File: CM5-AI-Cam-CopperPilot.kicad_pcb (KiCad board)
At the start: 6 copper layers, 55 x 40 mm, 90 parts, among them J1 IMX219_30P, J2 USB_A_Vertical, Q1 DMG1012T, Q2 DMG1012T, U1 RT9193-28GB, U2 RT9193-18GB, U3 RT9013-12, U4 STMPS2171STR, U5 MP1658GTF-Z, U6 FSUSB42MX, U7 STMPS2171STR, U8 STMPS2171STR, X1 OSC_24MHz

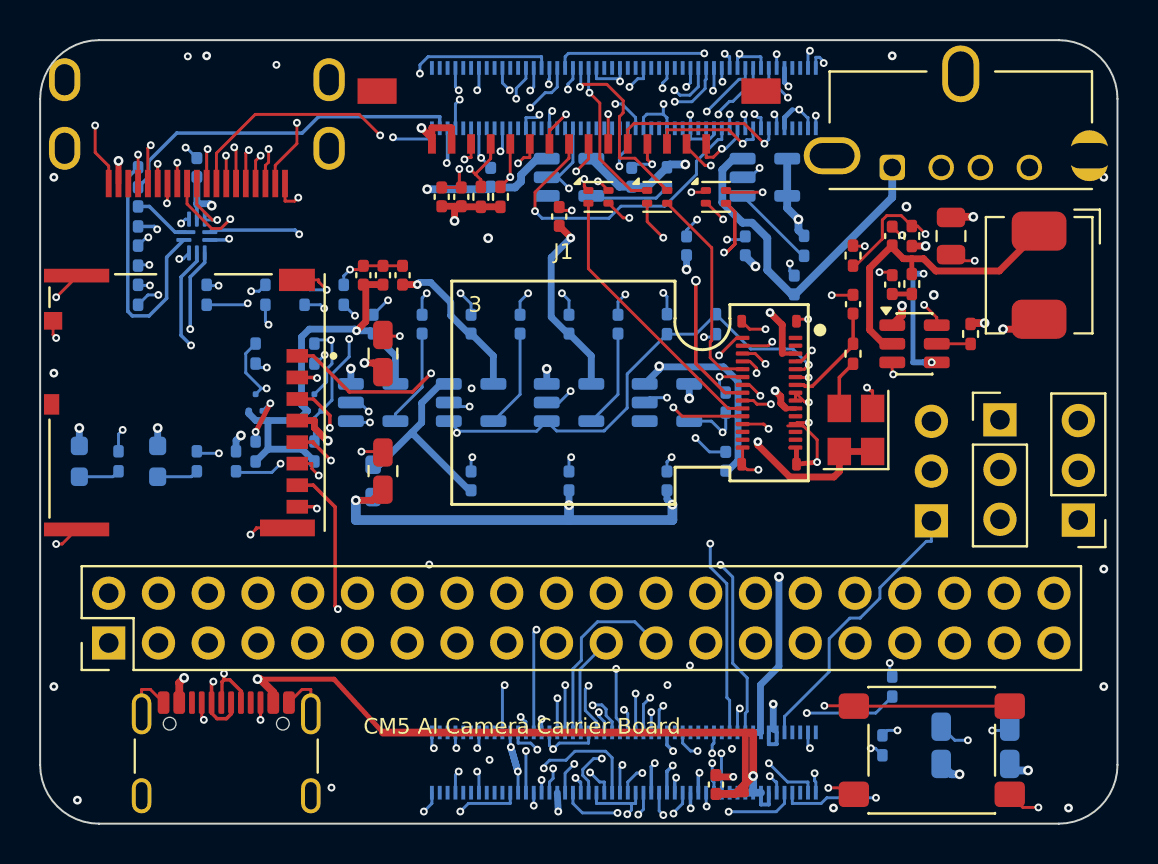
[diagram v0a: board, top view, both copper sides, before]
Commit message: fix(hardware): separate 100R MIPI/HDMI and 90R USB netclasses and resolve BOM/SCH/PCB review defects
- Assign HighSpeed_100R (100 Ohm diff: W=0.127mm, S=0.150mm -> 100.1 Ohm on JLC06161H-7628 stripline / 98.3 Ohm on JLC06161H-3313 microstrip) to MIPI CSI-2, MIPI DSI, and HDMI TMDS pairs, and HighSpeed_90R (90 Ohm diff: W=0.180mm, S=0.150mm -> 89.6 Ohm stripline / 88.7 Ohm microstrip) to USB 2.0 pairs in .kicad_pro, .kicad_pcb, and .kicad_dru.
- Synchronize .kicad_pcb stackup dielectric parameters with JLCPCB JLC06161H-7628 (0.2104mm prepreg, 0.4000mm core, er=4.6).
- Restore C20 on 24 MHz camera MCLK from 0.1uF (72.3 kHz cutoff) to 10pF (C32949, fc=723 MHz) and correct LCSC codes for R20 (C25803 61.9k), U3 (C47773 1.2V LDO), U1 (C15075 2.8V LDO), U5 (C2960187 MP1658GTF-Z), HDMI1 (C424662), L1-L3 (C110443), C21 (C1534 330pF), and U6 (FSUSB42UMX C11145).
- Exclude DNP straps R31, R32, R33 from BOM and CPL (--exclude-dnp) so CM5 Wi-Fi and Bluetooth remain enabled.
- Repair missing pad coordinates in CM5.pretty/R_0402_1005Metric.kicad_mod, TF1 SMD attribute, and 3D model  paths, and expand PyTest suite to 29 tests.

Co-Authored-By: CopperPilot <noreply@copperpilot.ai>
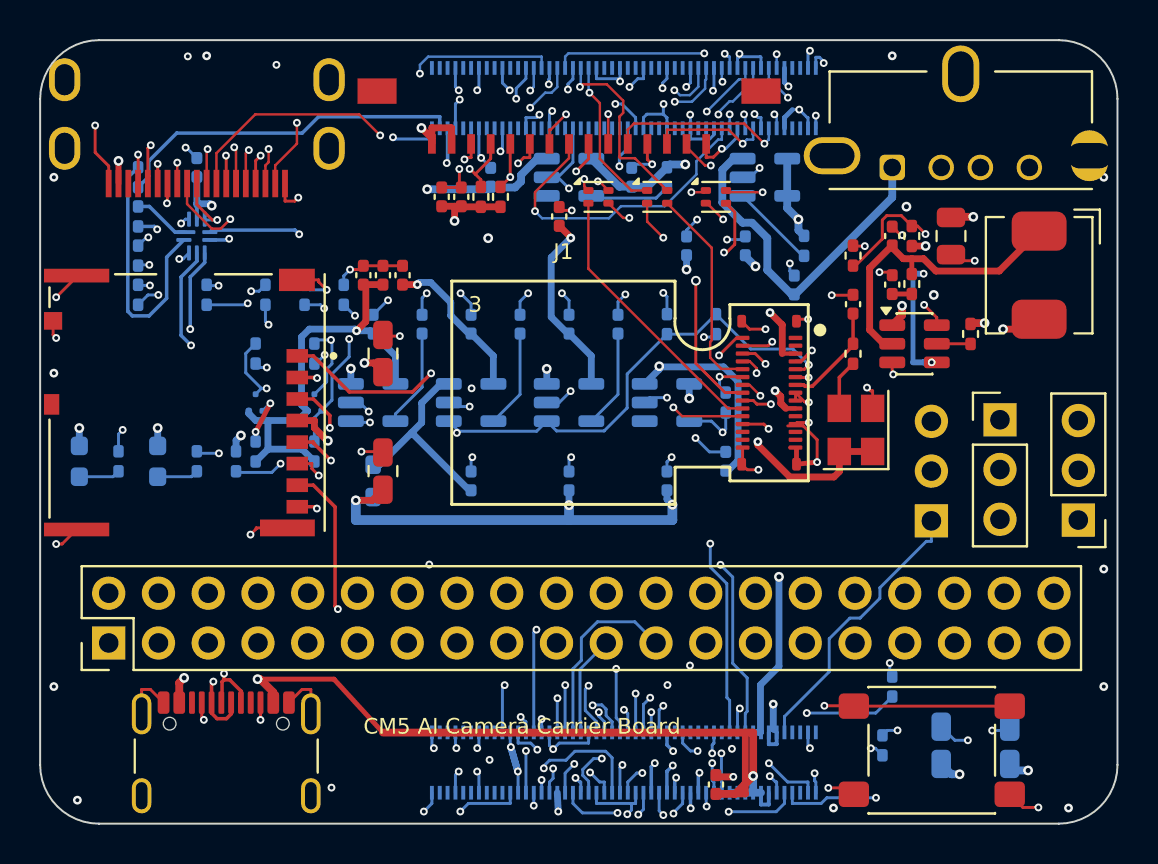
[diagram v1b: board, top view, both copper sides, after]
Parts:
- C10, C14, C3: value 100nF -> 0.1uF
- C20: value 0.1uF -> 10pF
- U6: value FSUSB42MX -> FSUSB42UMX
